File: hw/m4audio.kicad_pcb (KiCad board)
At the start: 2 copper layers, 49.5 x 49.5 mm, 76 parts, among them J1 JACK_TRS, J11 CONN_01X03, J2 JACK_TRS, J21 CONN_01X03, P1 CONN_01X02, P2 USB_OTG, P3 CONN_02X05, P4 CONN_01X08, P5 CONN_01X03, U1 LD1117S33TR, U2 STM32F405RG, U3 AD8542, U4 WM8731, Y1 Crystal

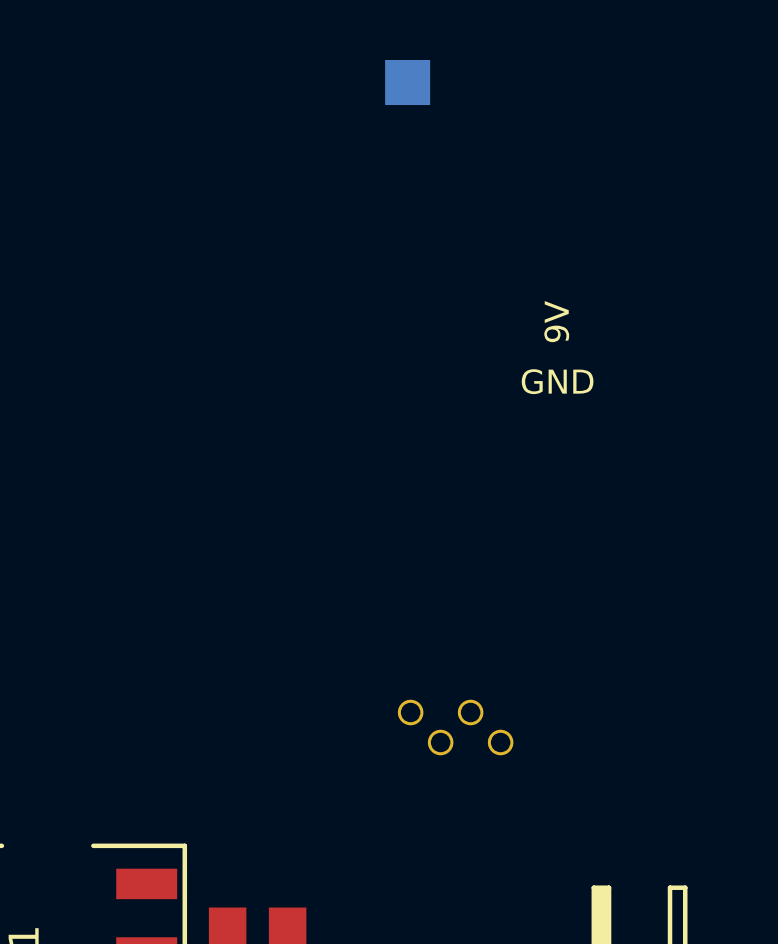
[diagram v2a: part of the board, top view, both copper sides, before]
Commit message: Make TPs a bit larger
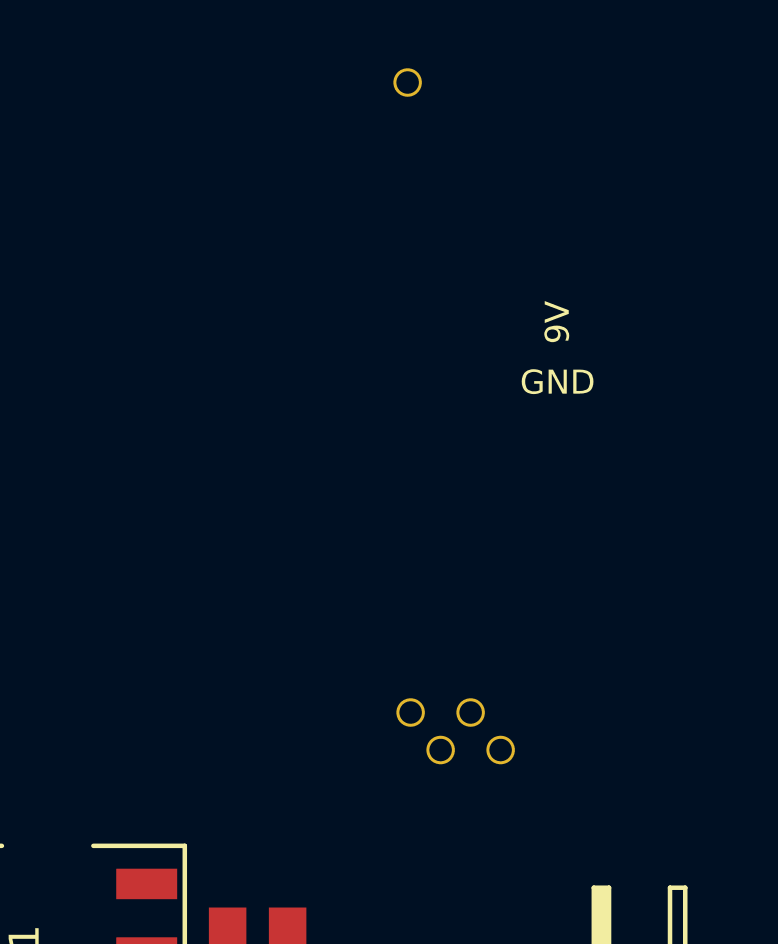
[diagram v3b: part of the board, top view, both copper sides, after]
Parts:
- TP1: footprint Measurement_Points:Measurement_Point_Square-SMD-Pad_Small -> Jonas_Connectors:TP_0.7mm
- TP5, TP6, TP7, TP8: footprint Jonas_Connectors:TP_0.6mm -> Jonas_Connectors:TP_0.7mm
- moved TP5 0.25 mm to (177.1, 109.8)
- moved TP6 0.25 mm to (179.1, 109.8)
- turned TP1 to 270 degrees
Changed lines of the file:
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@@
     (36 B.SilkS user)
     (37 F.SilkS user)
-    (38 B.Mask user)
-    (39 F.Mask user)
+    (38 B.Mask user hide)
+    (39 F.Mask user hide)
     (40 Dwgs.User user)
     (41 Cmts.User user)
@@
     )
   )
-  (module Measurement_Points:Measurement_Point_Square-SMD-Pad_Small (layer B.Cu)
-    (at 176 87.5)
-    (descr "Mesurement Point, Square, SMD Pad,  1.5mm x 1.5mm,")
-    (tags "Mesurement Point, Square, SMD Pad, 1.5mm x 1.5mm,")
-    (fp_text reference TP1 (at -3 0) (layer B.SilkS)
-      (effects (font (size 1 1) (thickness 0.15)) (justify mirror))
-    )
-    (fp_text value TST (at 2.54 -3.81) (layer B.Fab)
-      (effects (font (size 1 1) (thickness 0.15)) (justify mirror))
-    )
-    (pad 1 smd rect (at 0 0) (size 1.50114 1.50114) (layers B.Cu B.Paste B.Mask)
-      (net 56 "Net-(C2-Pad1)"))
-  )
   (module Capacitors_SMD:C_0805_HandSoldering (layer F.Cu)
     (at 128 96 270)
@@
     )
   )
-  (module Jonas_Connectors:TP_0.6mm (layer B.Cu)
-    (at 177.1 109.5 90)
-    (fp_text reference TP5 (at 1.75 0 90) (layer B.SilkS)
-      (effects (font (size 0.6 0.6) (thickness 0.1)) (justify mirror))
-    )
-    (fp_text value TST (at 0.25 1.25 90) (layer B.Fab) hide
-      (effects (font (size 1 1) (thickness 0.15)) (justify mirror))
-    )
-    (fp_line (start 0.25 -0.5) (end -0.5 -0.5) (layer B.SilkS) (width 0.1))
-    (fp_line (start 0.75 0) (end 0.25 -0.5) (layer B.SilkS) (width 0.1))
-    (fp_line (start 0.25 0.5) (end 0.75 0) (layer B.SilkS) (width 0.1))
-    (fp_line (start -0.5 0.5) (end 0.25 0.5) (layer B.SilkS) (width 0.1))
-    (fp_line (start -0.5 0.5) (end -0.5 -0.5) (layer B.SilkS) (width 0.1))
-    (pad 1 thru_hole circle (at 0 0 90) (size 0.85 0.85) (drill 0.65) (layers *.Cu *.Mask)
-      (net 38 /audio/DACDAT))
-  )
-  (module Jonas_Connectors:TP_0.6mm (layer B.Cu)
-    (at 179.1 109.5 90)
-    (fp_text reference TP6 (at 1.75 0 90) (layer B.SilkS)
-      (effects (font (size 0.6 0.6) (thickness 0.1)) (justify mirror))
-    )
-    (fp_text value TST (at 0.25 1.25 90) (layer B.Fab) hide
-      (effects (font (size 1 1) (thickness 0.15)) (justify mirror))
-    )
-    (fp_line (start 0.25 -0.5) (end -0.5 -0.5) (layer B.SilkS) (width 0.1))
-    (fp_line (start 0.75 0) (end 0.25 -0.5) (layer B.SilkS) (width 0.1))
-    (fp_line (start 0.25 0.5) (end 0.75 0) (layer B.SilkS) (width 0.1))
-    (fp_line (start -0.5 0.5) (end 0.25 0.5) (layer B.SilkS) (width 0.1))
-    (fp_line (start -0.5 0.5) (end -0.5 -0.5) (layer B.SilkS) (width 0.1))
-    (pad 1 thru_hole circle (at 0 0 90) (size 0.85 0.85) (drill 0.65) (layers *.Cu *.Mask)
-      (net 40 /audio/ADCLR))
-  )
-  (module Jonas_Connectors:TP_0.6mm (layer B.Cu)
-    (at 178.1 108.5 270)
-    (fp_text reference TP7 (at 1.75 0 270) (layer B.SilkS)
-      (effects (font (size 0.6 0.6) (thickness 0.1)) (justify mirror))
-    )
-    (fp_text value TST (at 0.25 1.25 270) (layer B.Fab) hide
-      (effects (font (size 1 1) (thickness 0.15)) (justify mirror))
-    )
-    (fp_line (start 0.25 -0.5) (end -0.5 -0.5) (layer B.SilkS) (width 0.1))
-    (fp_line (start 0.75 0) (end 0.25 -0.5) (layer B.SilkS) (width 0.1))
-    (fp_line (start 0.25 0.5) (end 0.75 0) (layer B.SilkS) (width 0.1))
-    (fp_line (start -0.5 0.5) (end 0.25 0.5) (layer B.SilkS) (width 0.1))
-    (fp_line (start -0.5 0.5) (end -0.5 -0.5) (layer B.SilkS) (width 0.1))
-    (pad 1 thru_hole circle (at 0 0 270) (size 0.85 0.85) (drill 0.65) (layers *.Cu *.Mask)
-      (net 39 /audio/ADCDAT))
-  )
-  (module Jonas_Connectors:TP_0.6mm (layer B.Cu)
-    (at 176.1 108.5 270)
-    (fp_text reference TP8 (at 1.75 0 270) (layer B.SilkS)
-      (effects (font (size 0.6 0.6) (thickness 0.1)) (justify mirror))
-    )
-    (fp_text value TST (at 0.25 1.25 270) (layer B.Fab) hide
-      (effects (font (size 1 1) (thickness 0.15)) (justify mirror))
-    )
-    (fp_line (start 0.25 -0.5) (end -0.5 -0.5) (layer B.SilkS) (width 0.1))
-    (fp_line (start 0.75 0) (end 0.25 -0.5) (layer B.SilkS) (width 0.1))
-    (fp_line (start 0.25 0.5) (end 0.75 0) (layer B.SilkS) (width 0.1))
-    (fp_line (start -0.5 0.5) (end 0.25 0.5) (layer B.SilkS) (width 0.1))
-    (fp_line (start -0.5 0.5) (end -0.5 -0.5) (layer B.SilkS) (width 0.1))
-    (pad 1 thru_hole circle (at 0 0 270) (size 0.85 0.85) (drill 0.65) (layers *.Cu *.Mask)
-      (net 37 /audio/BCLK))
-  )
   (module Oddities:NetTie-I_Connected_SMD (layer F.Cu)
     (at 166 127)
@@
       (net 56 "Net-(C2-Pad1)"))
   )
+  (module Jonas_Connectors:TP_0.7mm (layer B.Cu)
+    (at 176 87.5 270)
+    (fp_text reference TP1 (at 2 0 360) (layer B.SilkS)
+      (effects (font (size 0.6 0.6) (thickness 0.1)) (justify mirror))
+    )
+    (fp_text value TST (at 0.25 1.25 270) (layer B.Fab) hide
+      (effects (font (size 1 1) (thickness 0.15)) (justify mirror))
+    )
+    (fp_line (start 0.3 -0.65) (end -0.65 -0.65) (layer B.SilkS) (width 0.08))
+    (fp_line (start 0.95 0) (end 0.3 -0.65) (layer B.SilkS) (width 0.08))
+    (fp_line (start 0.3 0.65) (end 0.95 0) (layer B.SilkS) (width 0.08))
+    (fp_line (start -0.65 0.65) (end 0.3 0.65) (layer B.SilkS) (width 0.08))
+    (fp_line (start -0.65 0.65) (end -0.65 -0.65) (layer B.SilkS) (width 0.08))
+    (pad 1 thru_hole circle (at 0 0 270) (size 0.95 0.95) (drill 0.75) (layers *.Cu *.Mask)
+      (net 56 "Net-(C2-Pad1)"))
+  )
+  (module Jonas_Connectors:TP_0.7mm (layer B.Cu)
+    (at 177.1 109.75 90)
+    (fp_text reference TP5 (at -1.25 0 180) (layer B.SilkS)
+      (effects (font (size 0.6 0.6) (thickness 0.1)) (justify mirror))
+    )
+    (fp_text value TST (at 0.25 1.25 90) (layer B.Fab) hide
+      (effects (font (size 1 1) (thickness 0.15)) (justify mirror))
+    )
+    (fp_line (start 0.3 -0.65) (end -0.65 -0.65) (layer B.SilkS) (width 0.08))
+    (fp_line (start 0.95 0) (end 0.3 -0.65) (layer B.SilkS) (width 0.08))
+    (fp_line (start 0.3 0.65) (end 0.95 0) (layer B.SilkS) (width 0.08))
+    (fp_line (start -0.65 0.65) (end 0.3 0.65) (layer B.SilkS) (width 0.08))
+    (fp_line (start -0.65 0.65) (end -0.65 -0.65) (layer B.SilkS) (width 0.08))
+    (pad 1 thru_hole circle (at 0 0 90) (size 0.95 0.95) (drill 0.75) (layers *.Cu *.Mask)
+      (net 38 /audio/DACDAT))
+  )
+  (module Jonas_Connectors:TP_0.7mm (layer B.Cu)
+    (at 179.1 109.75 90)
+    (fp_text reference TP6 (at -1.25 0 180) (layer B.SilkS)
+      (effects (font (size 0.6 0.6) (thickness 0.1)) (justify mirror))
+    )
+    (fp_text value TST (at 0.25 1.25 90) (layer B.Fab) hide
+      (effects (font (size 1 1) (thickness 0.15)) (justify mirror))
+    )
+    (fp_line (start 0.3 -0.65) (end -0.65 -0.65) (layer B.SilkS) (width 0.08))
+    (fp_line (start 0.95 0) (end 0.3 -0.65) (layer B.SilkS) (width 0.08))
+    (fp_line (start 0.3 0.65) (end 0.95 0) (layer B.SilkS) (width 0.08))
+    (fp_line (start -0.65 0.65) (end 0.3 0.65) (layer B.SilkS) (width 0.08))
+    (fp_line (start -0.65 0.65) (end -0.65 -0.65) (layer B.SilkS) (width 0.08))
+    (pad 1 thru_hole circle (at 0 0 90) (size 0.95 0.95) (drill 0.75) (layers *.Cu *.Mask)
+      (net 40 /audio/ADCLR))
+  )
+  (module Jonas_Connectors:TP_0.7mm (layer B.Cu)
+    (at 178.1 108.5 270)
+    (fp_text reference TP7 (at -1.25 0.1 360) (layer B.SilkS)
+      (effects (font (size 0.6 0.6) (thickness 0.1)) (justify mirror))
+    )
+    (fp_text value TST (at 0.25 1.25 270) (layer B.Fab) hide
+      (effects (font (size 1 1) (thickness 0.15)) (justify mirror))
+    )
+    (fp_line (start 0.3 -0.65) (end -0.65 -0.65) (layer B.SilkS) (width 0.08))
+    (fp_line (start 0.95 0) (end 0.3 -0.65) (layer B.SilkS) (width 0.08))
+    (fp_line (start 0.3 0.65) (end 0.95 0) (layer B.SilkS) (width 0.08))
+    (fp_line (start -0.65 0.65) (end 0.3 0.65) (layer B.SilkS) (width 0.08))
+    (fp_line (start -0.65 0.65) (end -0.65 -0.65) (layer B.SilkS) (width 0.08))
+    (pad 1 thru_hole circle (at 0 0 270) (size 0.95 0.95) (drill 0.75) (layers *.Cu *.Mask)
+      (net 39 /audio/ADCDAT))
+  )
+  (module Jonas_Connectors:TP_0.7mm (layer B.Cu)
+    (at 176.1 108.5 270)
+    (fp_text reference TP8 (at -1.25 0 360) (layer B.SilkS)
+      (effects (font (size 0.6 0.6) (thickness 0.1)) (justify mirror))
+    )
+    (fp_text value TST (at 0.25 1.25 270) (layer B.Fab) hide
+      (effects (font (size 1 1) (thickness 0.15)) (justify mirror))
+    )
+    (fp_line (start 0.3 -0.65) (end -0.65 -0.65) (layer B.SilkS) (width 0.08))
+    (fp_line (start 0.95 0) (end 0.3 -0.65) (layer B.SilkS) (width 0.08))
+    (fp_line (start 0.3 0.65) (end 0.95 0) (layer B.SilkS) (width 0.08))
+    (fp_line (start -0.65 0.65) (end 0.3 0.65) (layer B.SilkS) (width 0.08))
+    (fp_line (start -0.65 0.65) (end -0.65 -0.65) (layer B.SilkS) (width 0.08))
+    (pad 1 thru_hole circle (at 0 0 270) (size 0.95 0.95) (drill 0.75) (layers *.Cu *.Mask)
+      (net 37 /audio/BCLK))
+  )
   (gr_line (start 160.75 137) (end 160.75 93) (layer Edge.Cuts) (width 0.1))

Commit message: Board...
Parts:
- added C27: 100n, Capacitors_SMD:C_0805_HandSoldering, F.Cu at (143.0, 114.0)
- added C28: DNP, Capacitors_ThroughHole:C_Radial_D8_L11.5_P3.5, F.Cu at (157.8, 121.8)
- added G***: LOGO, elemental:elemental-25.4mm, B.Cu at (122.5, 107.0)
- added G***: LOGO, elemental:elemental-4mm, F.Cu at (108.2, 86.8)
- added P6: CONN_01X04, Pin_Headers:Pin_Header_Angled_1x04, F.Cu at (114.9, 108.0)
- added TP10: TST, Jonas_Connectors:TP_0.7mm, B.Cu at (134.0, 113.0)
- added TP11: TST, Jonas_Connectors:TP_0.7mm, B.Cu at (136.5, 113.0)
- added TP12: TST, Jonas_Connectors:TP_0.7mm, B.Cu at (135.2, 113.0)
- added TP13: TST, Jonas_Connectors:TP_0.7mm, B.Cu at (144.5, 105.5)
- added TP14: TST, Jonas_Connectors:TP_0.7mm, B.Cu at (156.5, 133.0)
- added TP15: TST, Jonas_Connectors:TP_0.7mm, B.Cu at (152.0, 124.8)
- added TP16: TST, Jonas_Connectors:TP_0.7mm, B.Cu at (138.8, 115.8)
- added TP2: TST, Jonas_Connectors:TP_0.7mm, B.Cu at (138.5, 113.0)
- added TP9: TST, Jonas_Connectors:TP_0.7mm, B.Cu at (157.0, 127.8)
- D11, D21: footprint LEDs:LED-0805 -> LEDs:LED-3MM; moved to F.Cu
- P1: footprint Pin_Headers:Pin_Header_Angled_1x02 -> Pin_Headers:Pin_Header_Straight_1x02
- TP3, TP4: footprint Measurement_Points:Measurement_Point_Square-SMD-Pad_Small -> Jonas_Connectors:TP_0.7mm
- W2, W3, W4: footprint Oddities:NetTie-I_Connected_SMD -> Jonas_Connectors:net_tie_0805; moved to B.Cu
- moved TP1 64.4 mm to (119.0, 117.5), turned to 90 degrees
- moved OSHW 57.2 mm to (147.8, 98.0), turned to 290 degrees
- moved REF** 42.7 mm to (130.0, 126.0), turned to 250 degrees
- moved D1 38.8 mm to (146.0, 91.5), turned to 180 degrees
- moved D11 36.4 mm to (139.5, 92.5), turned to 0 degrees
- moved TP6 36.1 mm to (143.0, 109.8), turned to 180 degrees
- moved R8 35.0 mm to (146.0, 93.5), turned to 0 degrees
- moved TP7 33.6 mm to (144.5, 108.0), turned to 0 degrees
- moved TP5 32.7 mm to (144.5, 106.8), turned to 0 degrees
- moved TP8 31.6 mm to (144.5, 109.2), turned to 0 degrees
- moved W3 30.8 mm to (153.5, 106.5), turned to 270 degrees
- moved W1 29.6 mm to (150.0, 92.0), turned to 90 degrees
- moved P1 29.3 mm to (159.0, 107.0), turned to 0 degrees
- moved R7 28.6 mm to (147.5, 98.0), turned to 180 degrees
- moved D3 27.8 mm to (153.0, 108.0), turned to 180 degrees
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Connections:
- net /9V renamed /VSUPPLY
- net Net-(C25-Pad1) renamed /VCAP1
- net Net-(C26-Pad1) renamed /VCAP2
- C2 pad 1: Net-(C2-Pad1) -> /PWR_3V3
- R3 pad 1: GND -> Net-(R3-Pad1)
- R3 pad 2: Net-(R3-Pad2) -> GND
- TP1 pad 1: Net-(C2-Pad1) -> VAA
- U1 pad 2: Net-(C2-Pad1) -> /PWR_3V3
- U2 pad 43: Net-(R3-Pad2) -> Net-(R3-Pad1)
- U2 pad 58: (no net) -> /PB6
- U2 pad 59: (no net) -> /PB7
- U2 pad 61: (no net) -> /PB8
- W2 pad 2: Net-(C2-Pad1) -> /PWR_3V3
- W3 pad 2: Net-(C2-Pad1) -> /PWR_3V3
- W4 pad 2: Net-(C2-Pad1) -> /PWR_3V3
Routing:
- net GND: track 0.00 -> 170.9 mm, vias 0 -> 49
- net VDD: track 0.00 -> 147.2 mm, vias 0 -> 1
- net VAA: track 0.00 -> 104.2 mm, vias 0 -> 5
- net /audio/ADCR: track 0.00 -> 47.3 mm, vias 0 -> 1
- net /audio/ADCL: track 0.00 -> 42.4 mm, vias 0 -> 1
- net /audio/CS: track 0.00 -> 33.6 mm, vias 0 -> 1
- net /audio/SCLK: track 0.00 -> 33.0 mm, vias 0 -> 1
- net /MISC6: track 0.00 -> 31.9 mm, vias 0 -> 2
- net /SWDIO: track 0.00 -> 31.7 mm, vias 0 -> 2
- net /audio/MOSI: track 0.00 -> 31.1 mm, vias 0 -> 1
- net /audio/ADCLR: track 0.00 -> 30.6 mm, vias 0 -> 1
- net /audio/MCLK: track 0.00 -> 30.4 mm, vias 0 -> 1
- net /MISC5: track 0.00 -> 30.3 mm, vias 0 -> 2
- net /audio/AOUT_R: track 0.00 -> 30.0 mm
- net /audio/DACR: track 0.00 -> 30.0 mm, vias 0 -> 2
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- added copper zone on B.Cu, net /PWR_3V3
- added copper zone on B.Cu, net GND
- added copper zone on F.Cu, net GND
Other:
- board size 49.5 x 49.5 mm -> 49.7 x 49.7 mm
- net class Bigsupply: trace_width 0.3 -> 0.4
- net class Supply: trace_width 0.2 -> 0.25
- net class USB added: clearance 0.16, trace_width 0.3, via_dia 0.7, via_drill 0.3302
- board text added: "+"
- board text added: "-"
- board text added: "5-9V"
- board text added: "ADC"
- board text added: "BCLK"
- board text added: "Cortex Guitar Board"
- board text added: "Cortex Guitar Board rev.B Jonas Norling 2015"
- board text added: "DAC"
- board text added: "I²S"
- board text added: "LR"
- board text added: "MCLK"
- board text added: "PA8"
- board text added: "RX"
- board text added: "SPI"
- board text added: "TX"
- board text added: "USB-DFU"
- board text added: "VDD 3V3"
- board text added: "analog"
- board text added: "digital"
- board text added: "head- phone"
- board text added: "rev.B"
- board text removed: "+3.3V"
- board text removed: "9V"
- board text removed: "BOOT0"
- board text removed: "Cortex-M4 DSP board"
- board text removed: "Cortex-M4 DSP board rev.A Jonas Norling 2015"
- board text removed: "I2S"
- board text removed: "rev.A"

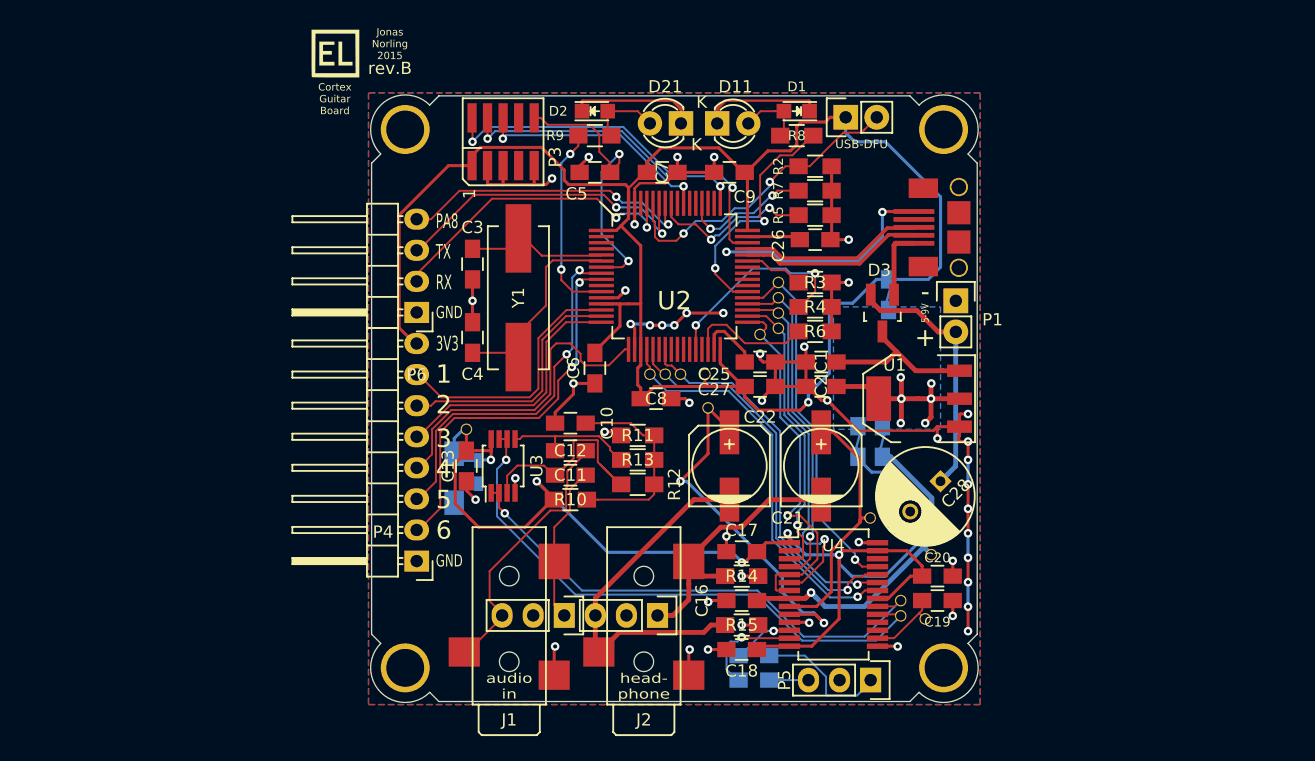
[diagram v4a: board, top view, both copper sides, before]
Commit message: Put a 2mm hole in the middle, adjust routing
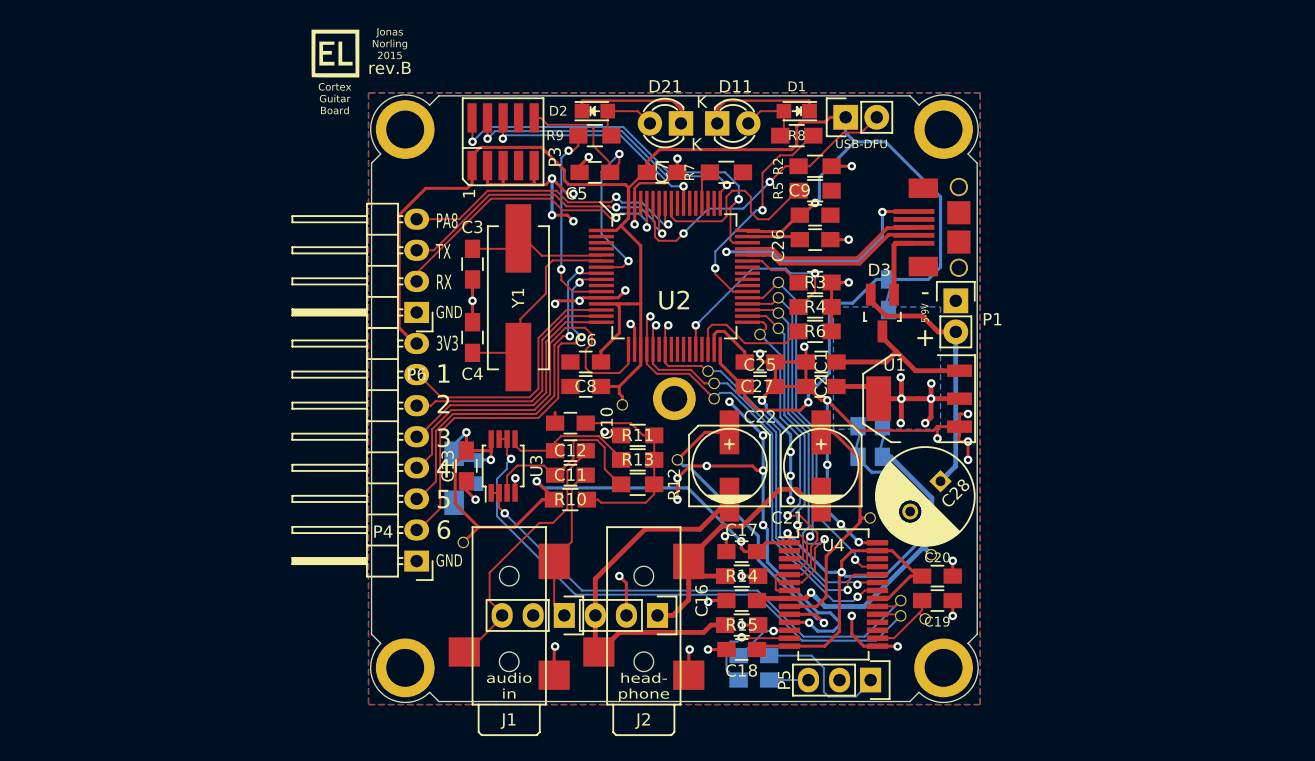
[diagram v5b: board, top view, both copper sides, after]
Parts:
- added REF**: MountingHole_2mm, Jonas_Mounting:MountingHole_2mm, F.Cu at (136.0, 115.0)
- REF** (x4): footprint Jonas_Mounting:MountingHole_3mm -> Jonas_Mounting:MountingHole_3mm_cogs
- moved TP1 9.25 mm to (118.8, 126.8), turned to 270 degrees
- moved C9 7.83 mm to (147.5, 100.0), turned to 0 degrees
- moved R7 7.40 mm to (140.2, 96.5)
- moved TP2 7.20 mm to (131.8, 115.5)
- moved C8 5.84 mm to (128.8, 114.0), turned to 180 degrees
- moved TP10 5.62 mm to (139.2, 115.0), turned to 0 degrees
- moved TP16 4.93 mm to (136.2, 120.0)
- moved TP12 4.07 mm to (139.2, 113.8), turned to 0 degrees
- moved TP11 2.26 mm to (138.8, 112.8), turned to 0 degrees
- moved R5 2.00 mm to (147.5, 98.0)
- moved C6 0.90 mm to (128.8, 112.0), turned to 180 degrees
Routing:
- net GND: track 170.9 -> 209.4 mm, vias 49 -> 54
- net Net-(R7-Pad2): track 10.9 -> 2.80 mm, vias 2 -> 0
- net /MISC4: track 26.5 -> 31.0 mm
- net /audio/CS: track 33.6 -> 36.7 mm, vias 1 -> 2
- net /audio/DACR: track 30.0 -> 27.2 mm, vias 2 -> 1
- net Net-(R5-Pad2): track 13.6 -> 16.3 mm, vias 2 -> 0
- net /audio/OPINL: track 19.5 -> 17.2 mm
- net /audio/SCLK: track 33.0 -> 35.3 mm, vias 1 -> 2
- net /audio/MOSI: track 31.1 -> 33.2 mm, vias 1 -> 2
- net /MISC6: track 31.9 -> 33.2 mm
- net /OSCOUT: track 17.2 -> 16.1 mm
- net /LED1: track 20.0 -> 18.8 mm
- net /audio/AOUT_R: track 30.0 -> 31.0 mm
- net /SWCLK: track 24.2 -> 25.1 mm
- net /audio/AOUT_L: track 22.7 -> 23.4 mm
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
